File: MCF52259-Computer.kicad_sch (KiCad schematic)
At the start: 17 parts, among them J1 Conn_02x10_Counter_Clockwise, Y1 8MHz

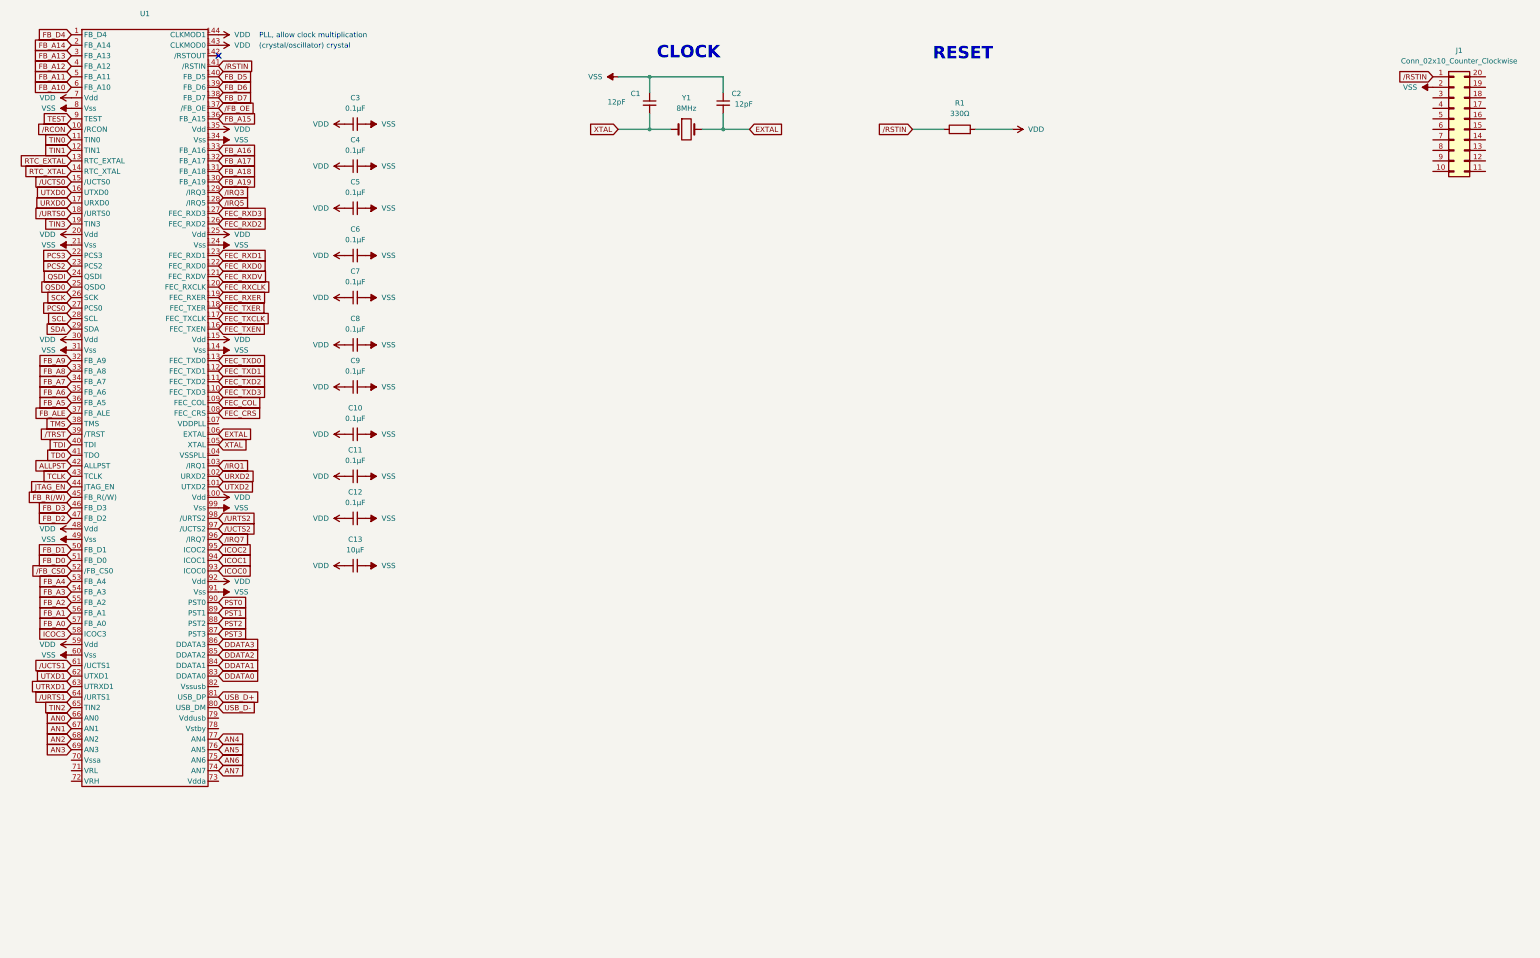
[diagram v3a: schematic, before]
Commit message: Added SD-Card
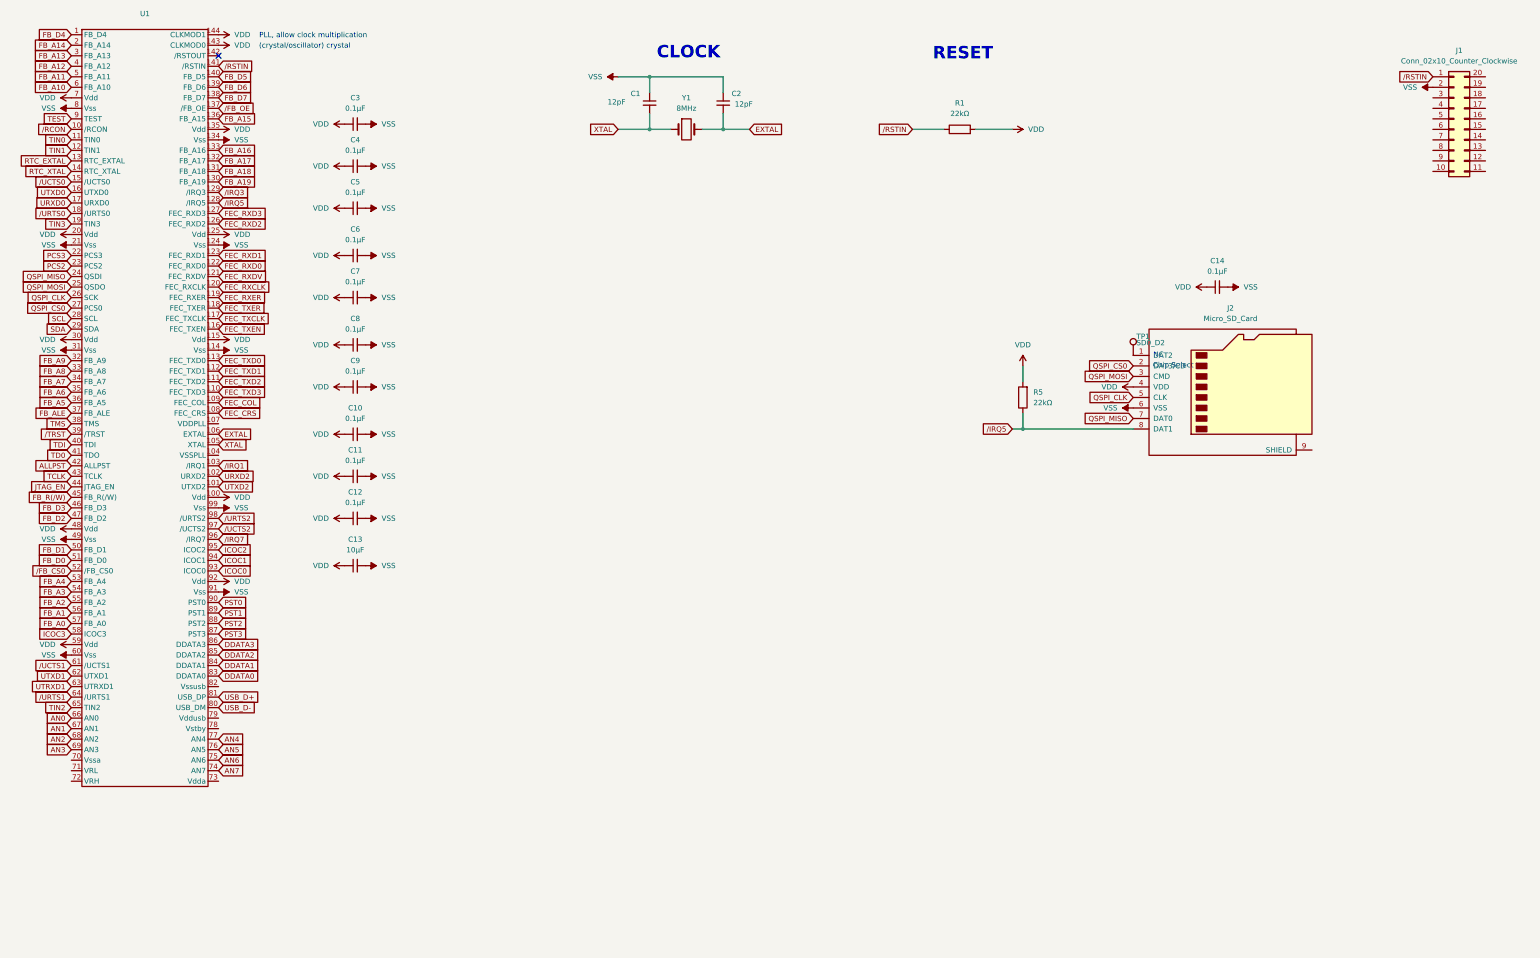
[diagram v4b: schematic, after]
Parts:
- added C14: 0.1µF, Capacitor_SMD:C_0805_2012Metric_Pad1.18x1.45mm_HandSolder, symbol Device:C_Small
- added J2: Micro_SD_Card, Connector_Card:microSD_HC_Wuerth_693072010801, symbol Connector:Micro_SD_Card
- added R5: 22kΩ, Resistor_SMD:R_0805_2012Metric_Pad1.20x1.40mm_HandSolder, symbol Device:R
- added TP1: SD0_D2, TestPoint:TestPoint_Pad_D1.0mm, symbol Connector:TestPoint
- R1: value 330Ω -> 22kΩ
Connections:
- net VDD: now also C14.1, J2.4 (VDD), R5.2
- net VSS: now also C14.2, J2.6 (VSS)
- net /IRQ5: now also J2.8 (DAT1), R5.1
- net PCS0 renamed QSPI_CS0
- net QSPI_CS0: now also J2.2 (DAT3/CD)
- net QSD0 renamed QSPI_MOSI
- net QSPI_MOSI: now also J2.3 (CMD)
- net QSDI renamed QSPI_MISO
- net QSPI_MISO: now also J2.7 (DAT0)
- net SCK renamed QSPI_CLK
- net QSPI_CLK: now also J2.5 (CLK)
- new net: J2.1 (DAT2), TP1.1
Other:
- note added: "Chip Select"
- note added: "NC"

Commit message: Added Second Micro SD-Card
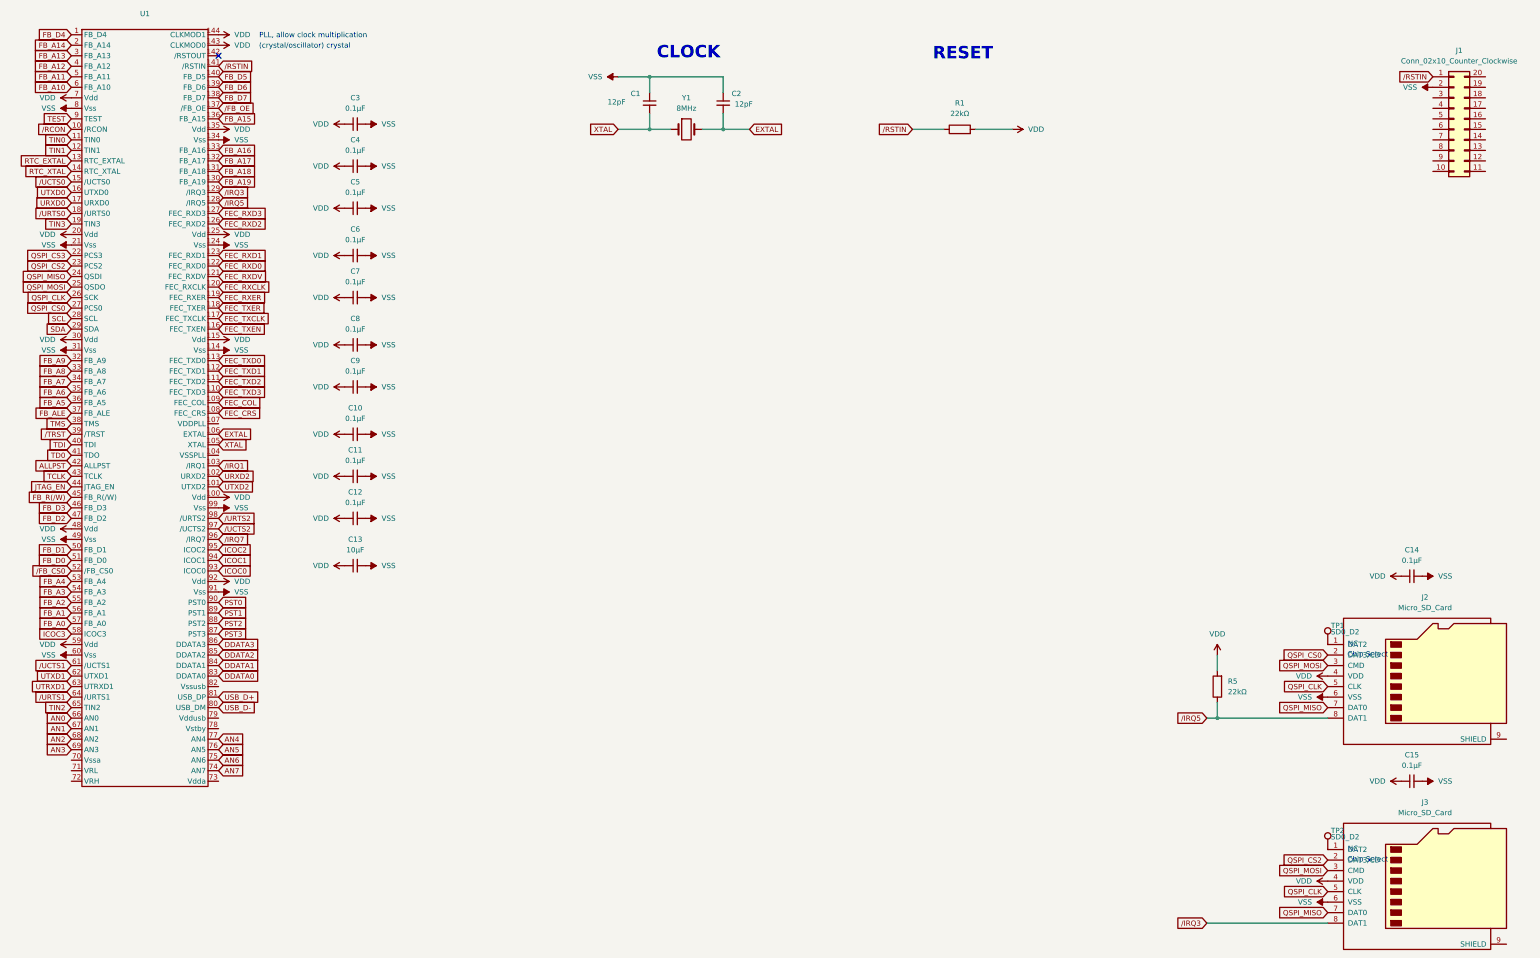
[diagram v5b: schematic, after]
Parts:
- added C15: 0.1µF, Capacitor_SMD:C_0805_2012Metric_Pad1.18x1.45mm_HandSolder, symbol Device:C_Small
- added J3: Micro_SD_Card, Connector_Card:microSD_HC_Wuerth_693072010801, symbol Connector:Micro_SD_Card
- added TP2: SD0_D2, TestPoint:TestPoint_Pad_D1.0mm, symbol Connector:TestPoint
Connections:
- net QSPI_CLK: now also J3.5 (CLK)
- net QSPI_MISO: now also J3.7 (DAT0)
- net QSPI_MOSI: now also J3.3 (CMD)
- net VDD: now also C15.1, J3.4 (VDD)
- net VSS: now also C15.2, J3.6 (VSS)
- net /IRQ3: now also J3.8 (DAT1)
- net PCS2 renamed QSPI_CS2
- net QSPI_CS2: now also J3.2 (DAT3/CD)
- net PCS3 renamed QSPI_CS3
- new net: J3.1 (DAT2), TP2.1
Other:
- moved on the sheet: C14, J2, R5, TP1

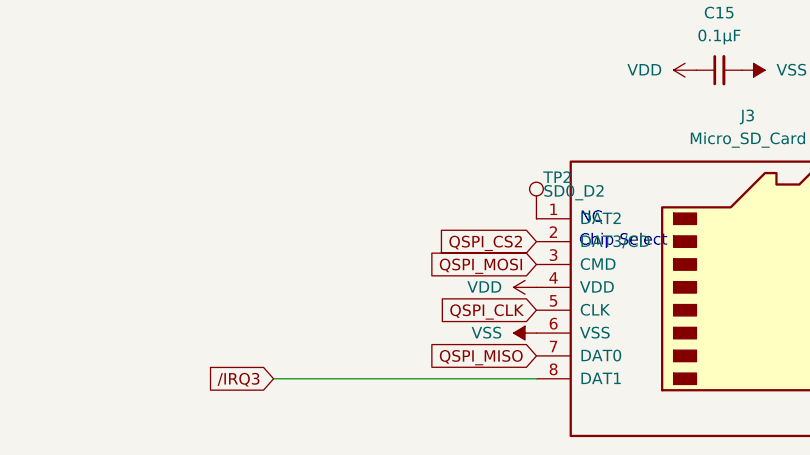
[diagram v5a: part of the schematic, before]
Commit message: Added Neccesary Pull-Up to IRQ3
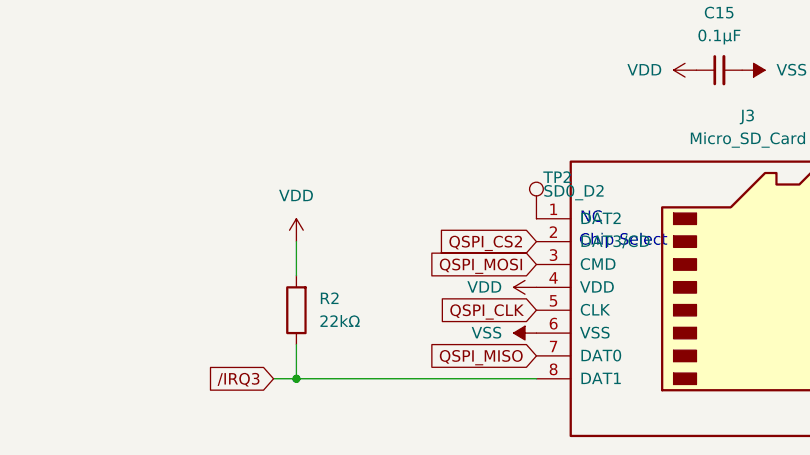
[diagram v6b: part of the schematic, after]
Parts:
- added R2: 22kΩ, Resistor_SMD:R_0805_2012Metric_Pad1.20x1.40mm_HandSolder, symbol Device:R
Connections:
- net VDD: now also R2.2
- net /IRQ3: now also R2.1
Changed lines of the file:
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@@
 	)
 	(junction
+		(at 325.12 229.87)
+		(diameter 0)
+		(color 0 0 0 0)
+	)
+	(junction
 		(at 187.96 38.1)
 		(diameter 0)
@@
 	(wire
 		(pts
-			(xy 322.58 229.87) (xy 351.79 229.87)
+			(xy 325.12 168.91) (xy 325.12 165.1)
 		)
 		(stroke
@@
 	(wire
 		(pts
-			(xy 325.12 168.91) (xy 325.12 165.1)
+			(xy 322.58 229.87) (xy 325.12 229.87)
 		)
 		(stroke
@@
 	(wire
 		(pts
+			(xy 325.12 218.44) (xy 325.12 214.63)
+		)
+		(stroke
+			(width 0)
+			(type default)
+		)
+	)
+	(wire
+		(pts
+			(xy 325.12 229.87) (xy 351.79 229.87)
+		)
+		(stroke
+			(width 0)
+			(type default)
+		)
+	)
+	(wire
+		(pts
 			(xy 325.12 180.34) (xy 351.79 180.34)
 		)
@@
 	(wire
 		(pts
+			(xy 325.12 226.06) (xy 325.12 229.87)
+		)
+		(stroke
+			(width 0)
+			(type default)
+		)
+	)
+	(wire
+		(pts
 			(xy 251.46 38.1) (xy 259.08 38.1)
 		)
@@
 	(symbol
 		(lib_id "power:VDD")
+		(at 325.12 214.63 0)
+		(unit 1)
+		(exclude_from_sim no)
+		(in_bom yes)
+		(on_board yes)
+		(dnp no)
+		(fields_autoplaced yes)
+		(property "Reference" "#PWR053"
+			(at 325.12 218.44 0)
+			(effects
+				(font
+					(size 1.27 1.27)
+				)
+				(hide yes)
+			)
+		)
+		(property "Value" "VDD"
+			(at 325.12 209.55 0)
+			(effects
+				(font
+					(size 1.27 1.27)
+				)
+			)
+		)
+		(property "Footprint" ""
+			(at 325.12 214.63 0)
+			(effects
+				(font
+					(size 1.27 1.27)
+				)
+				(hide yes)
+			)
+		)
+		(property "Datasheet" ""
+			(at 325.12 214.63 0)
+			(effects
+				(font
+					(size 1.27 1.27)
+				)
+				(hide yes)
+			)
+		)
+		(property "Description" "Power symbol creates a global label with name \"VDD\""
+			(at 325.12 214.63 0)
+			(effects
+				(font
+					(size 1.27 1.27)
+				)
+				(hide yes)
+			)
+		)
+		(pin "1"
+		)
+		(instances
+			(project "MCF52259-Computer"
+				(path "/c15ade3d-bb7e-4014-8f2f-451af952ec03"
+					(reference "#PWR053")
+					(unit 1)
+				)
+			)
+		)
+	)
+	(symbol
+		(lib_id "power:VDD")
 		(at 83.82 88.9 270)
 		(unit 1)
@@
 					(unit 1)
 				)
+			)
+		)
+	)
+	(symbol
+		(lib_id "Device:R")
+		(at 325.12 222.25 180)
+		(unit 1)
+		(exclude_from_sim no)
+		(in_bom yes)
+		(on_board yes)
+		(dnp no)
+		(fields_autoplaced yes)
+		(property "Reference" "R2"
+			(at 327.66 220.9799 0)
+			(effects
+				(font
+					(size 1.27 1.27)
+				)
+				(justify right)
+			)
+		)
+		(property "Value" "22kΩ"
+			(at 327.66 223.5199 0)
+			(effects
+				(font
+					(size 1.27 1.27)
+				)
+				(justify right)
+			)
+		)
+		(property "Footprint" "Resistor_SMD:R_0805_2012Metric_Pad1.20x1.40mm_HandSolder"
+			(at 326.898 222.25 90)
+			(effects
+				(font
+					(size 1.27 1.27)
+				)
+				(hide yes)
+			)
+		)
+		(property "Datasheet" "~"
+			(at 325.12 222.25 0)
+			(effects
+				(font
+					(size 1.27 1.27)
+				)
+				(hide yes)
+			)
+		)
+		(property "Description" "Resistor"
+			(at 325.12 222.25 0)
+			(effects
+				(font
+					(size 1.27 1.27)
+				)
+				(hide yes)
+			)
+		)
+		(pin "2"
+		)
+		(pin "1"
+		)
+		(instances
+			(project "MCF52259-Computer"
+				(path "/c15ade3d-bb7e-4014-8f2f-451af952ec03"
+					(reference "R2")
+					(unit 1)
+				)
